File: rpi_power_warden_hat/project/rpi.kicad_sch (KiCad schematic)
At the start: 15 parts, among them J10 Conn_01x06, J11 Conn_01x04, J4 Raspberry_Pi_4, J5 Conn_01x02, J6 Conn_01x04, J7 Conn_01x04, J8 Conn_01x04, J9 Conn_01x06, U3 CAT24C32WI-GT3

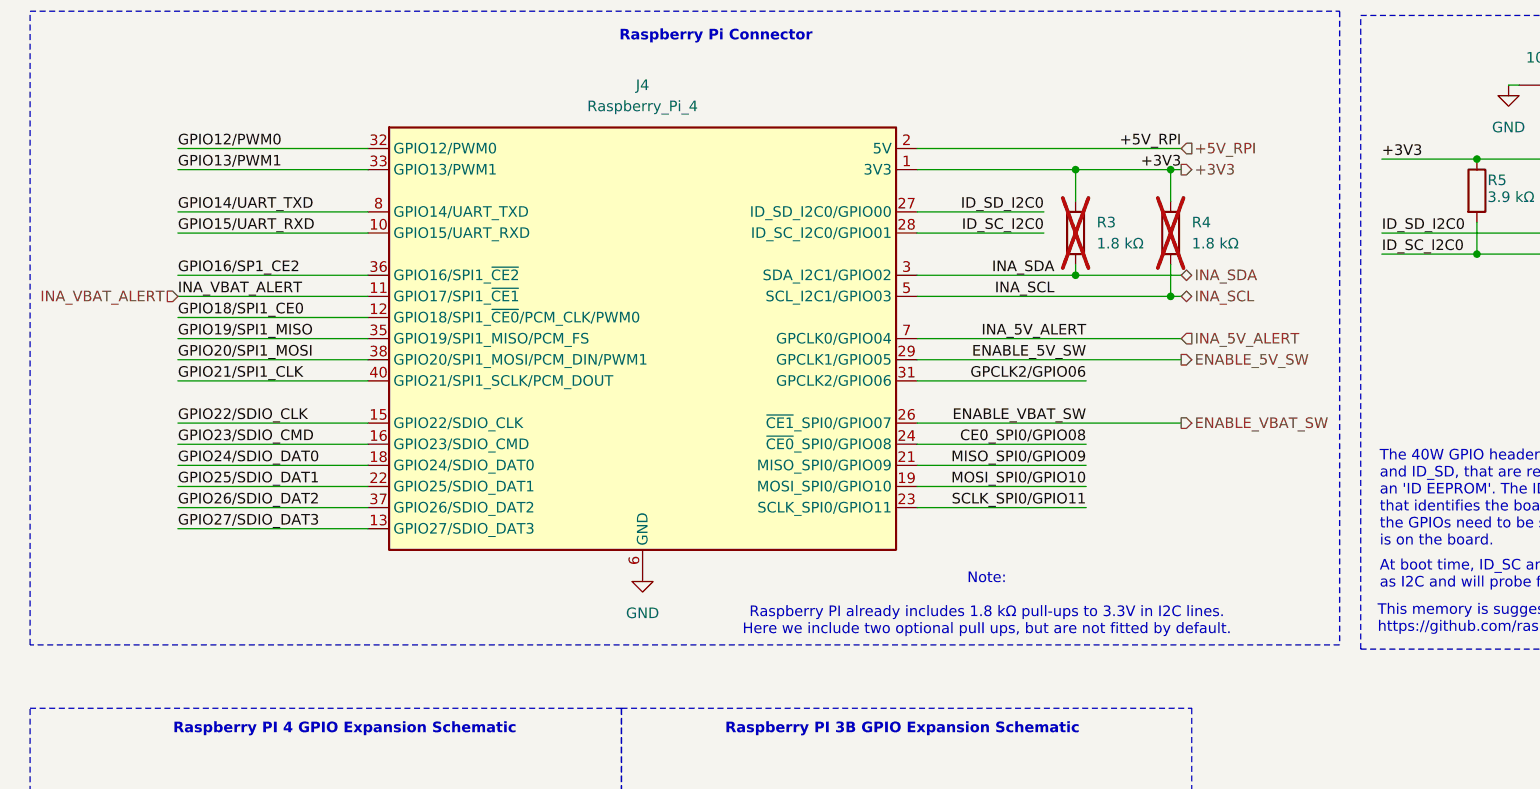
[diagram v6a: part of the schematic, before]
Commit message: add and gate in swiched power supplies enable
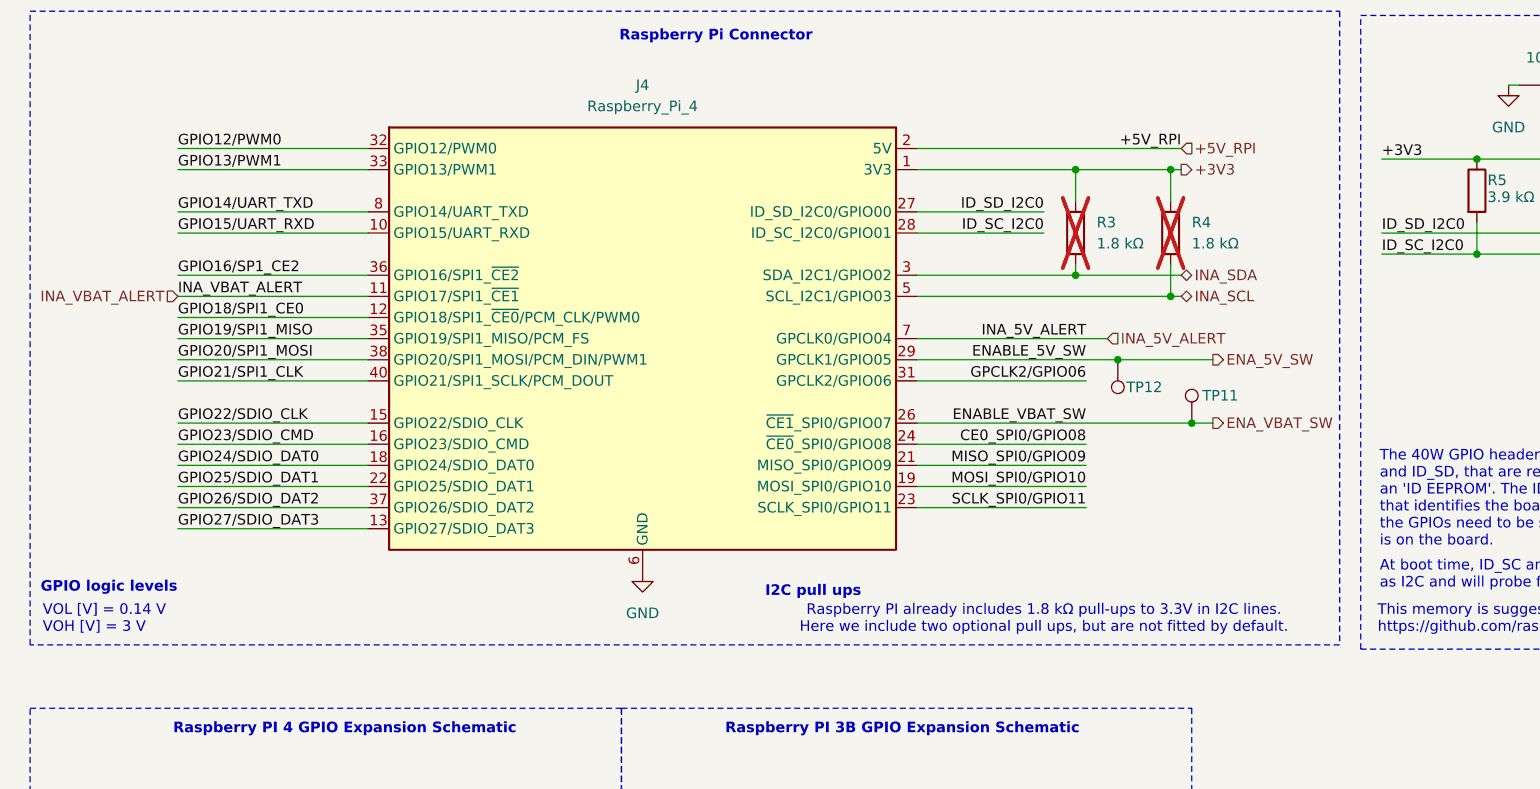
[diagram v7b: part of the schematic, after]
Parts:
- added TP11, TP12: TestPoint, TestPoint:TestPoint_Pad_D2.5mm, symbol Connector:TestPoint
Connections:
- net ENABLE_5V_SW renamed ENA_5V_SW
- net ENA_5V_SW: now also TP12.1
- net ENABLE_VBAT_SW renamed ENA_VBAT_SW
- net ENA_VBAT_SW: now also TP11.1
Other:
- note added: "GPIO logic levels"
- note added: "I2C pull ups"
- note added: "Raspberry PI already includes 1.8 kΩ pull-ups to 3.3V in I2C lines. Here we include two optional pull ups, but are not fitted by default."
- note added: "VOL [V] = 0.14 V VOH [V] = 3 V"
- note removed: "Note: Raspberry PI already includes 1.8 kΩ pull-ups to 3.3V in I2C lines. Here we include two optional pull ups, but are not fitted by default."
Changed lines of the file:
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@@
 	)
 	(junction
+		(at 154.94 87.63)
+		(diameter 0)
+		(color 0 0 0 0)
+	)
+	(junction
 		(at 234.95 59.69)
 		(diameter 0)
@@
 	)
 	(junction
+		(at 146.05 80.01)
+		(diameter 0)
+		(color 0 0 0 0)
+	)
+	(junction
 		(at 262.89 45.72)
 		(diameter 0)
@@
 	(wire
 		(pts
+			(xy 146.05 80.01) (xy 157.48 80.01)
+		)
+		(stroke
+			(width 0)
+			(type default)
+		)
+	)
+	(wire
+		(pts
 			(xy 33.02 77.47) (xy 55.88 77.47)
 		)
@@
 	(wire
 		(pts
-			(xy 121.92 87.63) (xy 153.67 87.63)
+			(xy 121.92 87.63) (xy 154.94 87.63)
 		)
 		(stroke
@@
 	(wire
 		(pts
-			(xy 121.92 80.01) (xy 153.67 80.01)
+			(xy 121.92 80.01) (xy 146.05 80.01)
 		)
 		(stroke
@@
 	(wire
 		(pts
+			(xy 154.94 87.63) (xy 157.48 87.63)
+		)
+		(stroke
+			(width 0)
+			(type default)
+		)
+	)
+	(wire
+		(pts
 			(xy 228.6 62.23) (xy 229.87 62.23)
 		)
@@
 	(wire
 		(pts
-			(xy 121.92 77.47) (xy 153.67 77.47)
+			(xy 121.92 77.47) (xy 144.78 77.47)
 		)
 		(stroke
@@
 		)
 	)
+	(text "GPIO logic levels"
+		(exclude_from_sim no)
+		(at 16.51 107.442 0)
+		(effects
+			(font
+				(size 1.27 1.27)
+				(thickness 0.254)
+				(bold yes)
+			)
+			(justify left)
+		)
+	)
 	(text "Extra GPIO headers"
 		(exclude_from_sim no)
@@
 		)
 	)
+	(text "VOL [V] = 0.14 V\nVOH [V] = 3 V"
+		(exclude_from_sim no)
+		(at 16.764 111.252 0)
+		(effects
+			(font
+				(size 1.27 1.27)
+			)
+			(justify left)
+		)
+	)
 	(text "This memory is suggested in HAT design guides:\nhttps://github.com/raspberrypi/hats/blob/master/designguide.md"
 		(exclude_from_sim no)
@@
 		)
 	)
-	(text "Note:\n\nRaspberry PI already includes 1.8 kΩ pull-ups to 3.3V in I2C lines.\nHere we include two optional pull ups, but are not fitted by default."
+	(text "Raspberry PI already includes 1.8 kΩ pull-ups to 3.3V in I2C lines.\nHere we include two optional pull ups, but are not fitted by default."
 		(exclude_from_sim no)
-		(at 130.302 109.474 0)
+		(at 137.16 111.252 0)
 		(effects
 			(font
@@
 		)
 	)
-	(text "Raspberry Pi Connector"
+	(text "I2C pull ups"
 		(exclude_from_sim no)
-		(at 86.106 41.148 0)
+		(at 103.632 107.95 0)
 		(effects
 			(font
@@
 		)
 	)
-	(text "Raspberry PI 3B GPIO Expansion Schematic\n"
+	(text "Raspberry Pi Connector"
 		(exclude_from_sim no)
-		(at 120.142 124.46 0)
+		(at 86.106 41.148 0)
 		(effects
 			(font
@@
 				(bold yes)
 			)
+			(justify left)
 		)
 	)
-	(label "INA_5V_ALERT"
-		(at 142.24 77.47 180)
+	(text "Raspberry PI 3B GPIO Expansion Schematic\n"
+		(exclude_from_sim no)
+		(at 120.142 124.46 0)
 		(effects
 			(font
 				(size 1.27 1.27)
+				(thickness 0.254)
+				(bold yes)
 			)
-			(justify right bottom)
 		)
 	)
-	(label "INA_SCL"
-		(at 138.43 72.39 180)
+	(label "INA_5V_ALERT"
+		(at 142.24 77.47 180)
 		(effects
 			(font
@@
 		)
 	)
-	(label "INA_SDA"
-		(at 138.43 69.85 180)
-		(effects
-			(font
-				(size 1.27 1.27)
-			)
-			(justify right bottom)
-		)
-	)
 	(label "GPIO24{slash}SDIO_DAT0"
 		(at 251.46 104.14 0)
@@
 		)
 	)
-	(label "+3V3"
-		(at 153.67 57.15 180)
-		(effects
-			(font
-				(size 1.27 1.27)
-			)
-			(justify right bottom)
-		)
-	)
 	(label "INA_VBAT_ALERT"
 		(at 33.02 72.39 0)
@@
 		)
 	)
-	(hierarchical_label "ENABLE_5V_SW"
+	(hierarchical_label "ENA_5V_SW"
 		(shape output)
-		(at 153.67 80.01 0)
+		(at 157.48 80.01 0)
 		(effects
 			(font
@@
 	(hierarchical_label "INA_5V_ALERT"
 		(shape input)
-		(at 153.67 77.47 0)
+		(at 144.78 77.47 0)
 		(effects
 			(font
@@
 		)
 	)
-	(hierarchical_label "ENABLE_VBAT_SW"
+	(hierarchical_label "ENA_VBAT_SW"
 		(shape output)
-		(at 153.67 87.63 0)
+		(at 157.48 87.63 0)
 		(effects
 			(font
@@
 					(unit 1)
 				)
+			)
+		)
+	)
+	(symbol
+		(lib_id "Connector:TestPoint")
+		(at 154.94 87.63 0)
+		(unit 1)
+		(exclude_from_sim no)
+		(in_bom yes)
+		(on_board yes)
+		(dnp no)
+		(property "Reference" "TP11"
+			(at 156.21 84.328 0)
+			(effects
+				(font
+					(size 1.27 1.27)
+				)
+				(justify left)
+			)
+		)
+		(property "Value" "TestPoint"
+			(at 157.48 85.5979 0)
+			(effects
+				(font
+					(size 1.27 1.27)
+				)
+				(justify left)
+				(hide yes)
+			)
+		)
+		(property "Footprint" "TestPoint:TestPoint_Pad_D2.5mm"
+			(at 160.02 87.63 0)
+			(effects
+				(font
+					(size 1.27 1.27)
+				)
+				(hide yes)
+			)
+		)
+		(property "Datasheet" "~"
+			(at 160.02 87.63 0)
+			(effects
+				(font
+					(size 1.27 1.27)
+				)
+				(hide yes)
+			)
+		)
+		(property "Description" "test point"
+			(at 154.94 87.63 0)
+			(effects
+				(font
+					(size 1.27 1.27)
+				)
+				(hide yes)
+			)
+		)
+		(pin "1"
+		)
+		(instances
+			(project "rpi_power_warden_hat"
+				(path "/8692c5de-a943-41e8-8e29-f6c5e99cda34/014d6471-91bd-4d51-9996-105480561d0c"
+					(reference "TP11")
+					(unit 1)
+				)
+			)
+		)
+	)
+	(symbol
+		(lib_id "Connector:TestPoint")
+		(at 146.05 80.01 0)
+		(mirror x)
+		(unit 1)
+		(exclude_from_sim no)
+		(in_bom yes)
+		(on_board yes)
+		(dnp no)
+		(property "Reference" "TP12"
+			(at 147.066 83.312 0)
+			(effects
+				(font
+					(size 1.27 1.27)
+				)
+				(justify left)
+			)
+		)
+		(property "Value" "TestPoint"
+			(at 148.59 82.0421 0)
+			(effects
+				(font
+					(size 1.27 1.27)
+				)
+				(justify left)
+				(hide yes)
+			)
+		)
+		(property "Footprint" "TestPoint:TestPoint_Pad_D2.5mm"
+			(at 151.13 80.01 0)
+			(effects
+				(font
+					(size 1.27 1.27)
+				)
+				(hide yes)
+			)
+		)
+		(property "Datasheet" "~"
+			(at 151.13 80.01 0)
+			(effects
+				(font
+					(size 1.27 1.27)
+				)
+				(hide yes)
+			)
+		)
+		(property "Description" "test point"
+			(at 146.05 80.01 0)
+			(effects
+				(font
+					(size 1.27 1.27)
+				)
+				(hide yes)
+			)
+		)
+		(pin "1"
+		)
+		(instances
+			(project "rpi_power_warden_hat"
+				(path "/8692c5de-a943-41e8-8e29-f6c5e99cda34/014d6471-91bd-4d51-9996-105480561d0c"
+					(reference "TP12")
+					(unit 1)
+				)
